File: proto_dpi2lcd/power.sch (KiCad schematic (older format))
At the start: 13 parts, among them J201 Barrel_Jack_Switch, U201 TLV71325PDBV, U202 ST1S10PHR, U203 TLV71312PDBV

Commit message: Progressing
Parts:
- added D201: Green, Diode_SMD:D_0805_2012Metric, symbol Device:LED
- added D202: P6SMBJ15A, Diode_SMD:D_SMB, symbol Device:D_Zener
- added R201: 200R, Resistor_SMD:R_0603_1608Metric, symbol Device:R
- C201: value 4u7 -> 10u/35V; footprint Capacitor_SMD:C_1206_3216Metric -> Capacitor_SMD:C_1210_3225Metric
- C206: value 22u -> 22u/25V
- renumbered R201 to R202, R202 to R203
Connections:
- net +12V: now also D202.1 (K)
- net +3V3: now also R201.1
- net GND: now also D201.1 (K), D202.2 (A)
- new net: D201.2 (A), R201.2
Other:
- moved on the sheet: C202, C203, C204, C205, C206, L201, R202, R203, U201, U202, U203

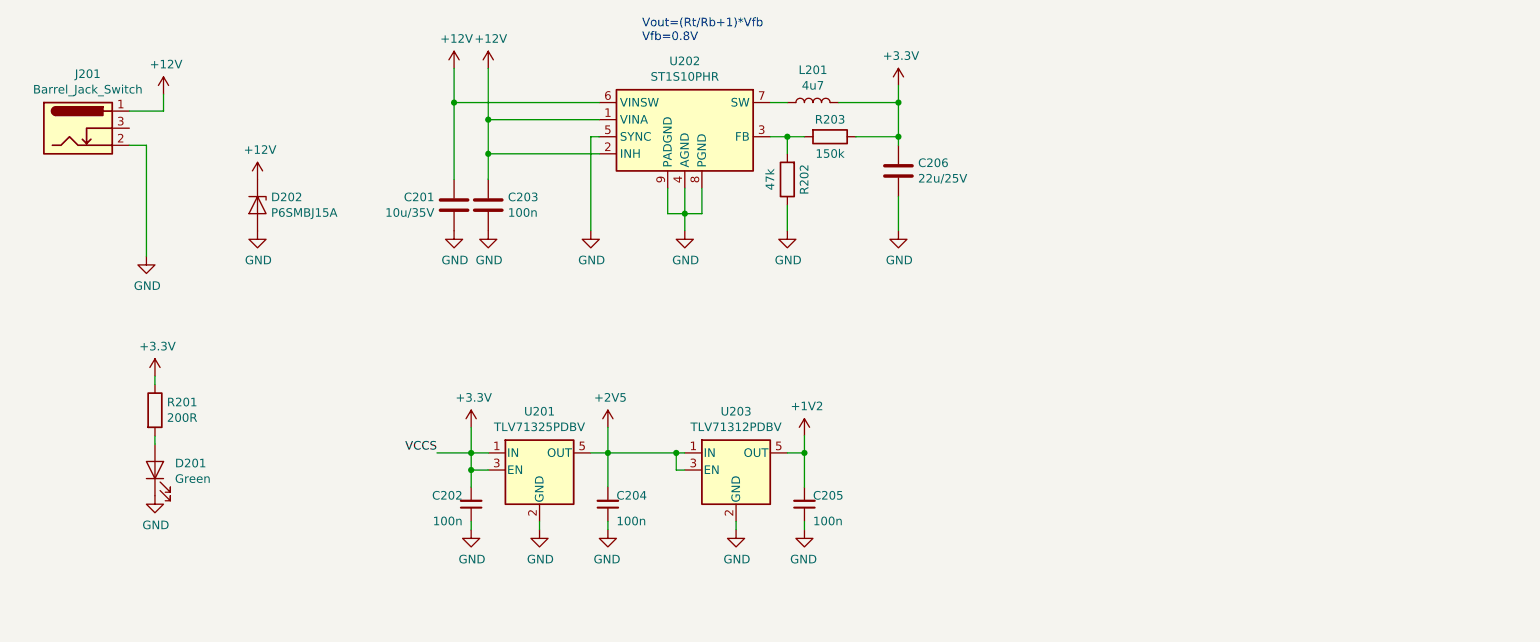
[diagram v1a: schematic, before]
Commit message: Work in progress
- Added BUCK for 12V->5V but inductors are TBD
 - Progress to the layout
 - some pin swapping has been done
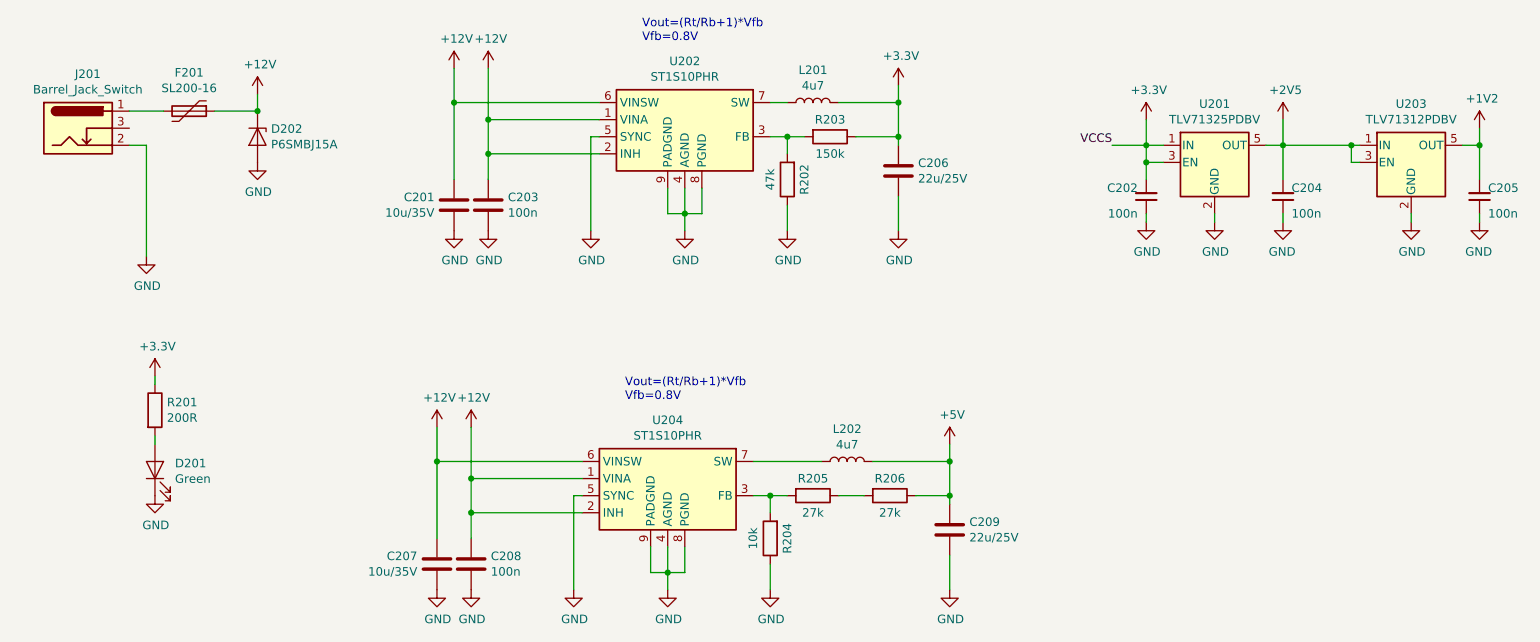
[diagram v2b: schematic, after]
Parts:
- added C207: 10u/35V, Capacitor_SMD:C_1210_3225Metric, symbol Device:C
- added C208: 100n, Capacitor_SMD:C_0603_1608Metric, symbol Device:C
- added C209: 22u/25V, Capacitor_SMD:C_1210_3225Metric, symbol Device:C
- added F201: SL200-16, Fuse:Fuse_2920_7451Metric_Pad2.10x5.45mm_HandSolder, symbol Device:Polyfuse
- added L202: 4u7, Inductor_SMD:L_12x12mm_H8mm, symbol Device:L
- added R204: 10k, Resistor_SMD:R_0603_1608Metric, symbol Device:R
- added R205, R206: 27k, Resistor_SMD:R_0603_1608Metric, symbol Device:R
- added U204: ST1S10PHR, Package_SO:TI_SO-PowerPAD-8, symbol Regulator_Switching:ST1S10PHR
- L201: footprint (none) -> Inductor_SMD:L_12x12mm_H8mm
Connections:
- net +12V: now also C207.2, C208.1, F201.1, U204.1 (VINA), U204.2 (INH), U204.6 (VINSW); no longer J201.1
- net GND: now also C207.1, C208.2, C209.2, R204.1, U204.4 (AGND), U204.5 (SYNC), U204.8 (PGND), U204.9 (PADGND)
- new net: R204.2, R205.2, U204.3 (FB)
- new net: L202.1, U204.7 (SW)
- new net: R205.1, R206.2
- new net: F201.2, J201.1
- new net +5V: C209.1, L202.2, R206.1
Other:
- moved on the sheet: C202, C204, C205, D202, U201, U203
